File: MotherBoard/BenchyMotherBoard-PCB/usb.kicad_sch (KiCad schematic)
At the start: 92 parts, among them J10 USB3_B, J11 USB3-PORT2, J12 USB3-PORT3, J13 USB3-PORT4, J14 USB3-PORT5, J15 USB-INTERNAL-PORT1, J16 TFT-DISPLAY, J17 USB-INTERNAL-PORT2, J9 USB3-PORT1, Q3 RQ5A030AP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

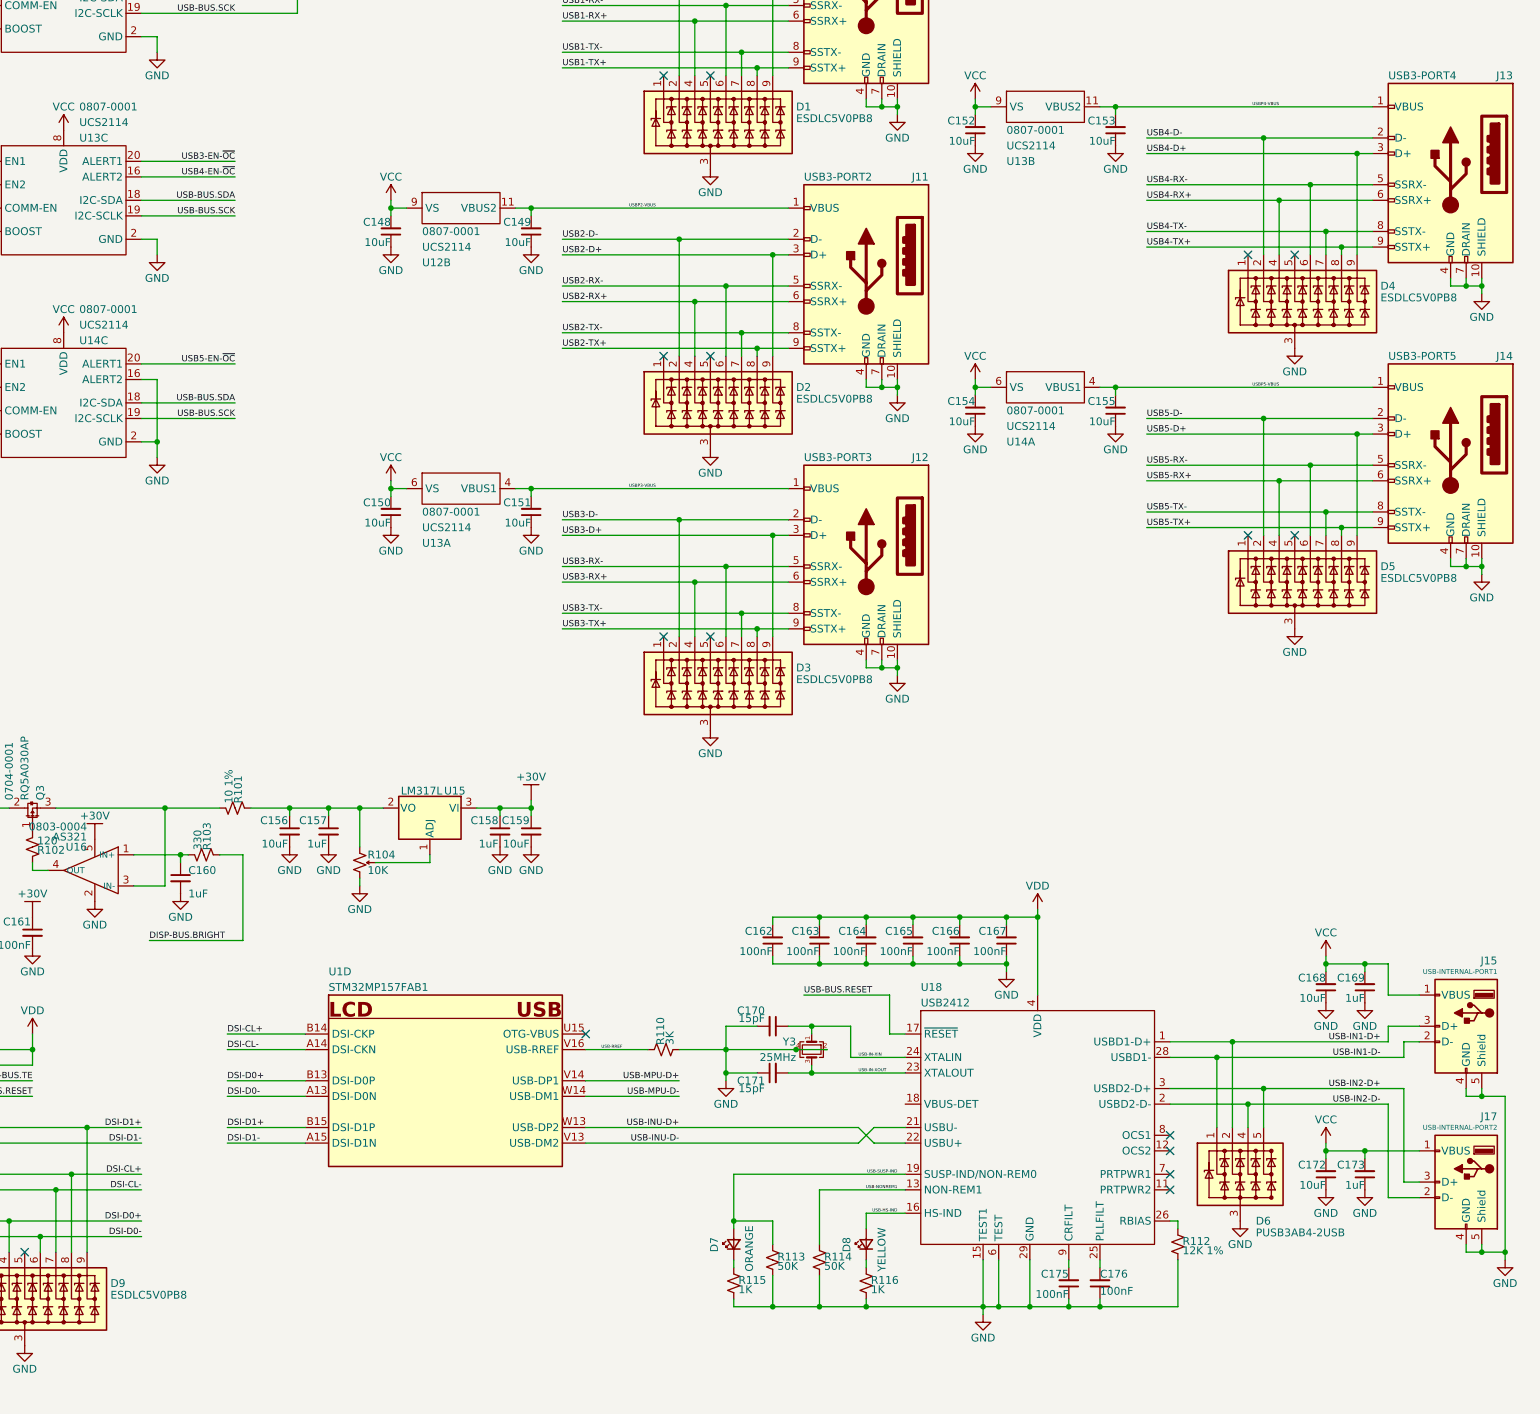
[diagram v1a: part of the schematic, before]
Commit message: Replace USB TVS W/ custom & finish DDR data layout
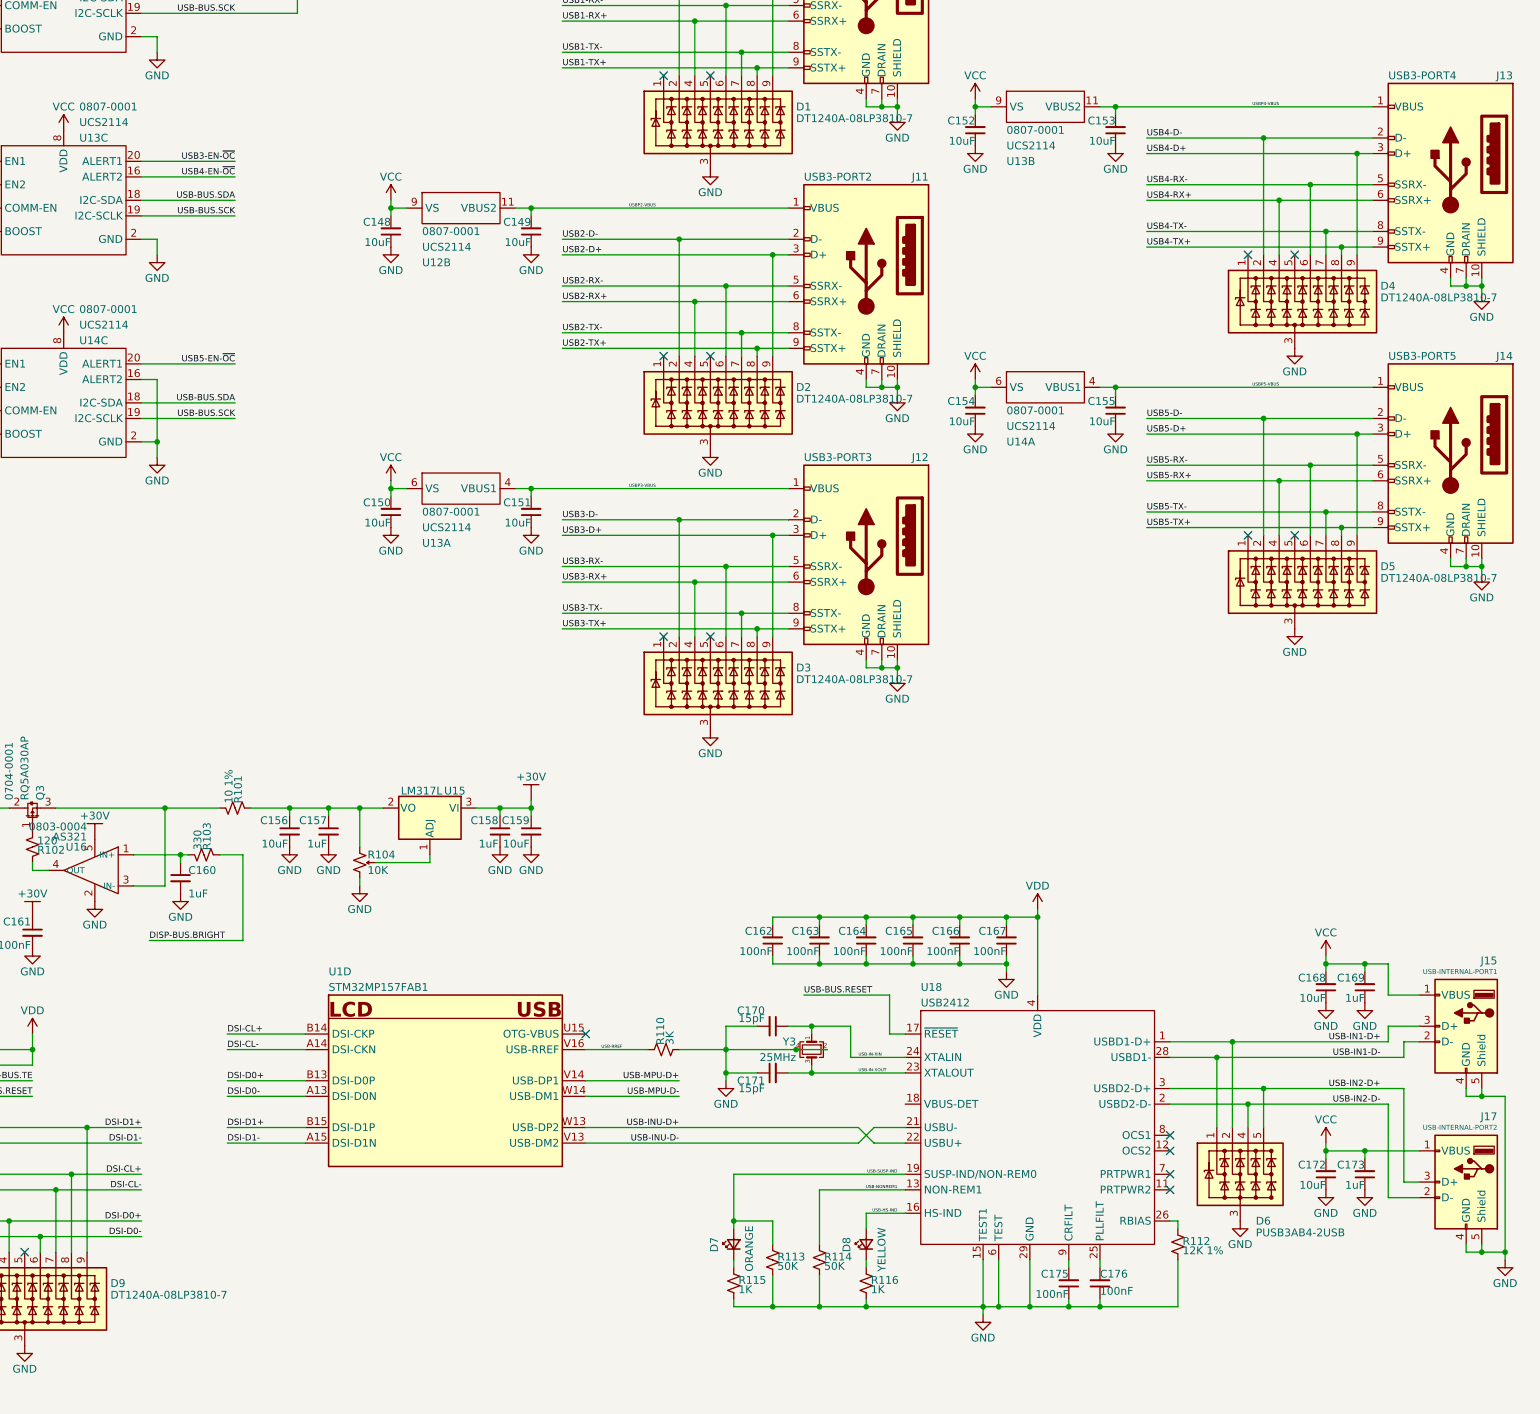
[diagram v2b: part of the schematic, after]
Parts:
- D1, D2, D3, D4, D5, D9: value ESDLC5V0PB8 -> DT1240A-08LP3810-7; footprint Package_DFN_QFN:UDFN-9_1.0x3.8mm_P0.5mm -> Daxxn_Packages:U-DFN3810-9; symbol Power_Protection:ESDLC5V0PB8 -> Daxxn_Protection:DT1240A-08LP3810-7
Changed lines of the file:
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@@
     )
   )
-  (symbol (lib_id "Power_Protection:ESDLC5V0PB8") (at 370.84 127 0) (unit 1)
+  (symbol (lib_id "Daxxn_Protection:DT1240A-08LP3810-7") (at 370.84 127 0) (unit 1)
     (in_bom yes) (on_board yes) (dnp no)
     (property "Reference" "D5" (at 384.81 124.46 0)
       (effects (font (size 1.27 1.27)) (justify left))
     )
-    (property "Value" "ESDLC5V0PB8" (at 384.81 126.365 0)
-      (effects (font (size 1.27 1.27)) (justify left))
-    )
-    (property "Footprint" "Package_DFN_QFN:UDFN-9_1.0x3.8mm_P0.5mm" (at 384.81 128.27 0)
+    (property "Value" "DT1240A-08LP3810-7" (at 384.81 126.365 0)
+      (effects (font (size 1.27 1.27)) (justify left))
+    )
+    (property "Footprint" "Daxxn_Packages:U-DFN3810-9" (at 384.81 128.27 0)
       (effects (font (size 1.27 1.27)) (justify left) hide)
     )
-    (property "Datasheet" "https://www.mccsemi.com/pdf/Products/ESDLC5V0PB8(DFN3810-9)-A.pdf" (at 375.285 126.365 0)
+    (property "Datasheet" "https://www.diodes.com/assets/Datasheets/DT1240A-08LP3810.pdf" (at 375.285 126.365 0)
       (effects (font (size 1.27 1.27)) hide)
     )
@@
     )
   )
-  (symbol (lib_id "Power_Protection:ESDLC5V0PB8") (at 275.59 97.79 0) (unit 1)
+  (symbol (lib_id "Daxxn_Protection:DT1240A-08LP3810-7") (at 275.59 97.79 0) (unit 1)
     (in_bom yes) (on_board yes) (dnp no)
     (property "Reference" "D2" (at 289.56 95.25 0)
       (effects (font (size 1.27 1.27)) (justify left))
     )
-    (property "Value" "ESDLC5V0PB8" (at 289.56 97.155 0)
-      (effects (font (size 1.27 1.27)) (justify left))
-    )
-    (property "Footprint" "Package_DFN_QFN:UDFN-9_1.0x3.8mm_P0.5mm" (at 289.56 99.06 0)
+    (property "Value" "DT1240A-08LP3810-7" (at 289.56 97.155 0)
+      (effects (font (size 1.27 1.27)) (justify left))
+    )
+    (property "Footprint" "Daxxn_Packages:U-DFN3810-9" (at 289.56 99.06 0)
       (effects (font (size 1.27 1.27)) (justify left) hide)
     )
-    (property "Datasheet" "https://www.mccsemi.com/pdf/Products/ESDLC5V0PB8(DFN3810-9)-A.pdf" (at 280.035 97.155 0)
+    (property "Datasheet" "https://www.diodes.com/assets/Datasheets/DT1240A-08LP3810.pdf" (at 280.035 97.155 0)
       (effects (font (size 1.27 1.27)) hide)
     )
@@
     )
   )
-  (symbol (lib_id "Power_Protection:ESDLC5V0PB8") (at 275.59 143.51 0) (unit 1)
+  (symbol (lib_id "Daxxn_Protection:DT1240A-08LP3810-7") (at 275.59 143.51 0) (unit 1)
     (in_bom yes) (on_board yes) (dnp no)
     (property "Reference" "D3" (at 289.56 140.97 0)
       (effects (font (size 1.27 1.27)) (justify left))
     )
-    (property "Value" "ESDLC5V0PB8" (at 289.56 142.875 0)
-      (effects (font (size 1.27 1.27)) (justify left))
-    )
-    (property "Footprint" "Package_DFN_QFN:UDFN-9_1.0x3.8mm_P0.5mm" (at 289.56 144.78 0)
+    (property "Value" "DT1240A-08LP3810-7" (at 289.56 142.875 0)
+      (effects (font (size 1.27 1.27)) (justify left))
+    )
+    (property "Footprint" "Daxxn_Packages:U-DFN3810-9" (at 289.56 144.78 0)
       (effects (font (size 1.27 1.27)) (justify left) hide)
     )
-    (property "Datasheet" "https://www.mccsemi.com/pdf/Products/ESDLC5V0PB8(DFN3810-9)-A.pdf" (at 280.035 142.875 0)
+    (property "Datasheet" "https://www.diodes.com/assets/Datasheets/DT1240A-08LP3810.pdf" (at 280.035 142.875 0)
       (effects (font (size 1.27 1.27)) hide)
     )
@@
     )
   )
-  (symbol (lib_id "Power_Protection:ESDLC5V0PB8") (at 163.83 243.84 0) (unit 1)
+  (symbol (lib_id "Daxxn_Protection:DT1240A-08LP3810-7") (at 163.83 243.84 0) (unit 1)
     (in_bom yes) (on_board yes) (dnp no)
     (property "Reference" "D9" (at 177.8 241.3 0)
       (effects (font (size 1.27 1.27)) (justify left))
     )
-    (property "Value" "ESDLC5V0PB8" (at 177.8 243.205 0)
-      (effects (font (size 1.27 1.27)) (justify left))
-    )
-    (property "Footprint" "Package_DFN_QFN:UDFN-9_1.0x3.8mm_P0.5mm" (at 177.8 245.11 0)
+    (property "Value" "DT1240A-08LP3810-7" (at 177.8 243.205 0)
+      (effects (font (size 1.27 1.27)) (justify left))
+    )
+    (property "Footprint" "Daxxn_Packages:U-DFN3810-9" (at 177.8 245.11 0)
       (effects (font (size 1.27 1.27)) (justify left) hide)
     )
-    (property "Datasheet" "https://www.mccsemi.com/pdf/Products/ESDLC5V0PB8(DFN3810-9)-A.pdf" (at 168.275 243.205 0)
+    (property "Datasheet" "https://www.diodes.com/assets/Datasheets/DT1240A-08LP3810.pdf" (at 168.275 243.205 0)
       (effects (font (size 1.27 1.27)) hide)
     )
@@
     )
   )
-  (symbol (lib_id "Power_Protection:ESDLC5V0PB8") (at 370.84 81.28 0) (unit 1)
+  (symbol (lib_id "Daxxn_Protection:DT1240A-08LP3810-7") (at 370.84 81.28 0) (unit 1)
     (in_bom yes) (on_board yes) (dnp no)
     (property "Reference" "D4" (at 384.81 78.74 0)
       (effects (font (size 1.27 1.27)) (justify left))
     )
-    (property "Value" "ESDLC5V0PB8" (at 384.81 80.645 0)
-      (effects (font (size 1.27 1.27)) (justify left))
-    )
-    (property "Footprint" "Package_DFN_QFN:UDFN-9_1.0x3.8mm_P0.5mm" (at 384.81 82.55 0)
+    (property "Value" "DT1240A-08LP3810-7" (at 384.81 80.645 0)
+      (effects (font (size 1.27 1.27)) (justify left))
+    )
+    (property "Footprint" "Daxxn_Packages:U-DFN3810-9" (at 384.81 82.55 0)
       (effects (font (size 1.27 1.27)) (justify left) hide)
     )
-    (property "Datasheet" "https://www.mccsemi.com/pdf/Products/ESDLC5V0PB8(DFN3810-9)-A.pdf" (at 375.285 80.645 0)
+    (property "Datasheet" "https://www.diodes.com/assets/Datasheets/DT1240A-08LP3810.pdf" (at 375.285 80.645 0)
       (effects (font (size 1.27 1.27)) hide)
     )
@@
     )
   )
-  (symbol (lib_id "Power_Protection:ESDLC5V0PB8") (at 275.59 52.07 0) (unit 1)
+  (symbol (lib_id "Daxxn_Protection:DT1240A-08LP3810-7") (at 275.59 52.07 0) (unit 1)
     (in_bom yes) (on_board yes) (dnp no)
     (property "Reference" "D1" (at 289.56 49.53 0)
       (effects (font (size 1.27 1.27)) (justify left))
     )
-    (property "Value" "ESDLC5V0PB8" (at 289.56 51.435 0)
-      (effects (font (size 1.27 1.27)) (justify left))
-    )
-    (property "Footprint" "Package_DFN_QFN:UDFN-9_1.0x3.8mm_P0.5mm" (at 289.56 53.34 0)
+    (property "Value" "DT1240A-08LP3810-7" (at 289.56 51.435 0)
+      (effects (font (size 1.27 1.27)) (justify left))
+    )
+    (property "Footprint" "Daxxn_Packages:U-DFN3810-9" (at 289.56 53.34 0)
       (effects (font (size 1.27 1.27)) (justify left) hide)
     )
-    (property "Datasheet" "https://www.mccsemi.com/pdf/Products/ESDLC5V0PB8(DFN3810-9)-A.pdf" (at 280.035 51.435 0)
-      (effects (font (size 1.27 1.27)) hide)
-    )
+    (property "Datasheet" "https://www.diodes.com/assets/Datasheets/DT1240A-08LP3810.pdf" (at 280.035 51.435 0)
+      (effects (font (size 1.27 1.27)) hide)
+    )

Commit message: REV1 - Finish layout and finalize pcb
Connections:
- net USB13-COMM: no longer R97.1, U14.3 (COMM-EN)
- new net USB14-COMM: R97.1, U14.3 (COMM-EN)
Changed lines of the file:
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@@
     (effects (font (size 1.016 1.016)) (justify right bottom))
   )
-  (label "USB13-COMM" (at 149.86 99.06 0) (fields_autoplaced)
+  (label "USB14-COMM" (at 149.86 99.06 0) (fields_autoplaced)
     (effects (font (size 0.5 0.5)) (justify left bottom))
   )

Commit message: Add volt meter PCB
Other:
- note added: "BUS BREAKOUT"
- note added: "DIRECT USB PORTS"
- note added: "DISPLAY"
- note added: "DOWNSTREAM PORTS"
- note added: "UPSTREAM PORT"
- note added: "USB HUB"
- note added: "USB HUB CTRL"
- note added: "USB POWER"
- moved on the sheet: C145, C146, C147, C148, C149, C150, C151, C152, C153, C154, C155, C156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

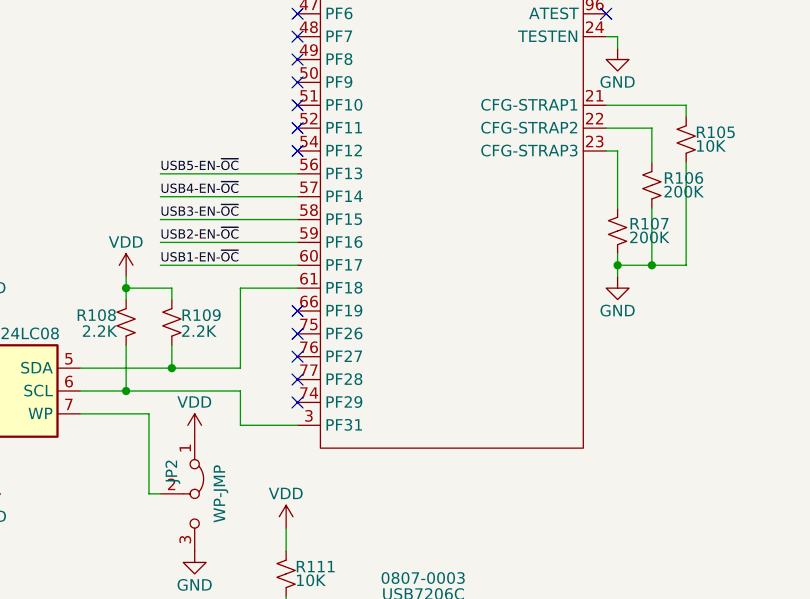
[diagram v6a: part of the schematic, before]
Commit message: Wrap up REV2 and add voltmeter gerbers
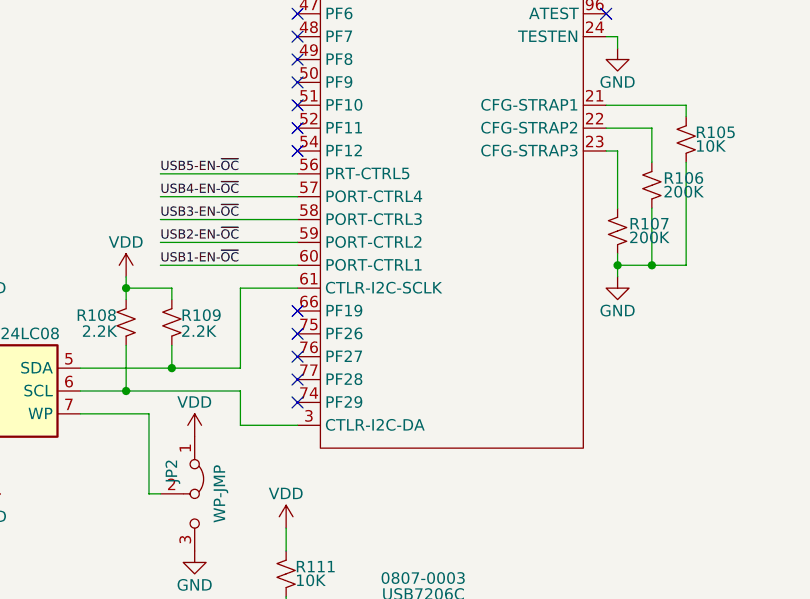
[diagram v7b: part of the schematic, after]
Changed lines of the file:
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@@
     (pin "23")
     (pin "24")
-    (pin "3")
+    (pin "3" (alternate "CTLR-I2C-DA"))
     (pin "44")
     (pin "45")
@@
     (pin "52")
     (pin "54")
-    (pin "56")
-    (pin "57")
-    (pin "58")
-    (pin "59")
-    (pin "60")
-    (pin "61")
+    (pin "56" (alternate "PRT-CTRL5"))
+    (pin "57" (alternate "PORT-CTRL4"))
+    (pin "58" (alternate "PORT-CTRL3"))
+    (pin "59" (alternate "PORT-CTRL2"))
+    (pin "60" (alternate "PORT-CTRL1"))
+    (pin "61" (alternate "CTLR-I2C-SCLK"))
     (pin "63")
     (pin "64")
@@
     (pin "23")
     (pin "24")
-    (pin "3")
+    (pin "3" (alternate "CTLR-I2C-DA"))
     (pin "44")
     (pin "45")
@@
     (pin "52")
     (pin "54")
-    (pin "56")
-    (pin "57")
-    (pin "58")
-    (pin "59")
-    (pin "60")
-    (pin "61")
+    (pin "56" (alternate "PRT-CTRL5"))
+    (pin "57" (alternate "PORT-CTRL4"))
+    (pin "58" (alternate "PORT-CTRL3"))
+    (pin "59" (alternate "PORT-CTRL2"))
+    (pin "60" (alternate "PORT-CTRL1"))
+    (pin "61" (alternate "CTLR-I2C-SCLK"))
     (pin "63")
     (pin "64")
@@
     (pin "23")
     (pin "24")
-    (pin "3")
+    (pin "3" (alternate "CTLR-I2C-DA"))
     (pin "44")
     (pin "45")
@@
     (pin "52")
     (pin "54")
-    (pin "56")
-    (pin "57")
-    (pin "58")
-    (pin "59")
-    (pin "60")
-    (pin "61")
+    (pin "56" (alternate "PRT-CTRL5"))
+    (pin "57" (alternate "PORT-CTRL4"))
+    (pin "58" (alternate "PORT-CTRL3"))
+    (pin "59" (alternate "PORT-CTRL2"))
+    (pin "60" (alternate "PORT-CTRL1"))
+    (pin "61" (alternate "CTLR-I2C-SCLK"))
     (pin "63")
     (pin "64")
